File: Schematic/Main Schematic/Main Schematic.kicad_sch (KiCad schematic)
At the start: 5 parts, among them J1 Conn_01x24_Socket, J2 Conn_01x10_Pin, J3 Conn_01x24_Socket, SW1 SW_Push

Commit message: Update
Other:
- sheet Sensor ports: added 3.3V; removed none
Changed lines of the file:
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@@
-    (stroke (width 0) (type default))
-  )
-  (wire (pts (xy 250.19 43.18) (xy 255.27 43.18))
     (stroke (width 0) (type default))
   )
@@
   )
   (wire (pts (xy 250.19 53.34) (xy 255.27 53.34))
+    (stroke (width 0) (type default))
+  )
+  (wire (pts (xy 250.19 43.18) (xy 255.2192 43.18))
     (stroke (width 0) (type default))
   )
@@
     (effects (font (size 1.27 1.27)) (justify left bottom))
   )
-  (label "PB7" (at 255.27 43.18 0) (fields_autoplaced)
-    (effects (font (size 1.27 1.27)) (justify left bottom))
-    (property "Intersheetrefs" "${INTERSHEET_REFS}" (at 259.8611 43.18 0)
+  (label "PB7" (at 255.2192 43.18 0) (fields_autoplaced)
+    (effects (font (size 1.27 1.27)) (justify left bottom))
+    (property "Intersheetrefs" "${INTERSHEET_REFS}" (at 259.8103 43.18 0)
       (effects (font (size 1.27 1.27)) (justify left) hide)
     )
@@
       (effects (font (size 1.27 1.27)) hide)
     )
+  )
+  (label "3.3V" (at 63.8048 97.7392 0) (fields_autoplaced)
+    (effects (font (size 1.27 1.27)) (justify left bottom))
   )
   (label "BOOT" (at 269.24 40.64 0) (fields_autoplaced)
@@
       (effects (font (size 1.27 1.27)) (justify right))
     )
+    (pin "3.3V" input (at 63.8048 97.7392 90)
+      (effects (font (size 1.27 1.27)) (justify right))
+    )

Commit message: Updat
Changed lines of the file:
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@@
     (effects (font (size 1.27 1.27)) (justify right bottom))
   )
-  (label "PB1" (at 218.44 76.2 180) (fields_autoplaced)
-    (effects (font (size 1.27 1.27)) (justify right bottom))
-    (property "Intersheetrefs" "${INTERSHEET_REFS}" (at 20.32 -64.77 0)
-      (effects (font (size 1.27 1.27)) hide)
+  (label "PB1" (at 218.44 76.2 0) (fields_autoplaced)
+    (effects (font (size 1.27 1.27)) (justify left bottom))
+    (property "Intersheetrefs" "${INTERSHEET_REFS}" (at 223.0311 76.2 0)
+      (effects (font (size 1.27 1.27)) (justify left) hide)
     )
   )
@@
     )
   )
-  (label "PA7" (at 218.44 71.12 180) (fields_autoplaced)
-    (effects (font (size 1.27 1.27)) (justify right bottom))
-    (property "Intersheetrefs" "${INTERSHEET_REFS}" (at 20.32 -64.77 0)
-      (effects (font (size 1.27 1.27)) hide)
+  (label "PA7" (at 218.44 71.12 0) (fields_autoplaced)
+    (effects (font (size 1.27 1.27)) (justify left bottom))
+    (property "Intersheetrefs" "${INTERSHEET_REFS}" (at 222.8497 71.12 0)
+      (effects (font (size 1.27 1.27)) (justify left) hide)
     )
   )
@@
     (effects (font (size 1.27 1.27)) (justify right bottom))
   )
-  (label "PB0" (at 218.44 73.66 180) (fields_autoplaced)
-    (effects (font (size 1.27 1.27)) (justify right bottom))
-    (property "Intersheetrefs" "${INTERSHEET_REFS}" (at 20.32 -64.77 0)
-      (effects (font (size 1.27 1.27)) hide)
+  (label "PB0" (at 218.44 73.66 0) (fields_autoplaced)
+    (effects (font (size 1.27 1.27)) (justify left bottom))
+    (property "Intersheetrefs" "${INTERSHEET_REFS}" (at 223.0311 73.66 0)
+      (effects (font (size 1.27 1.27)) (justify left) hide)
     )
   )

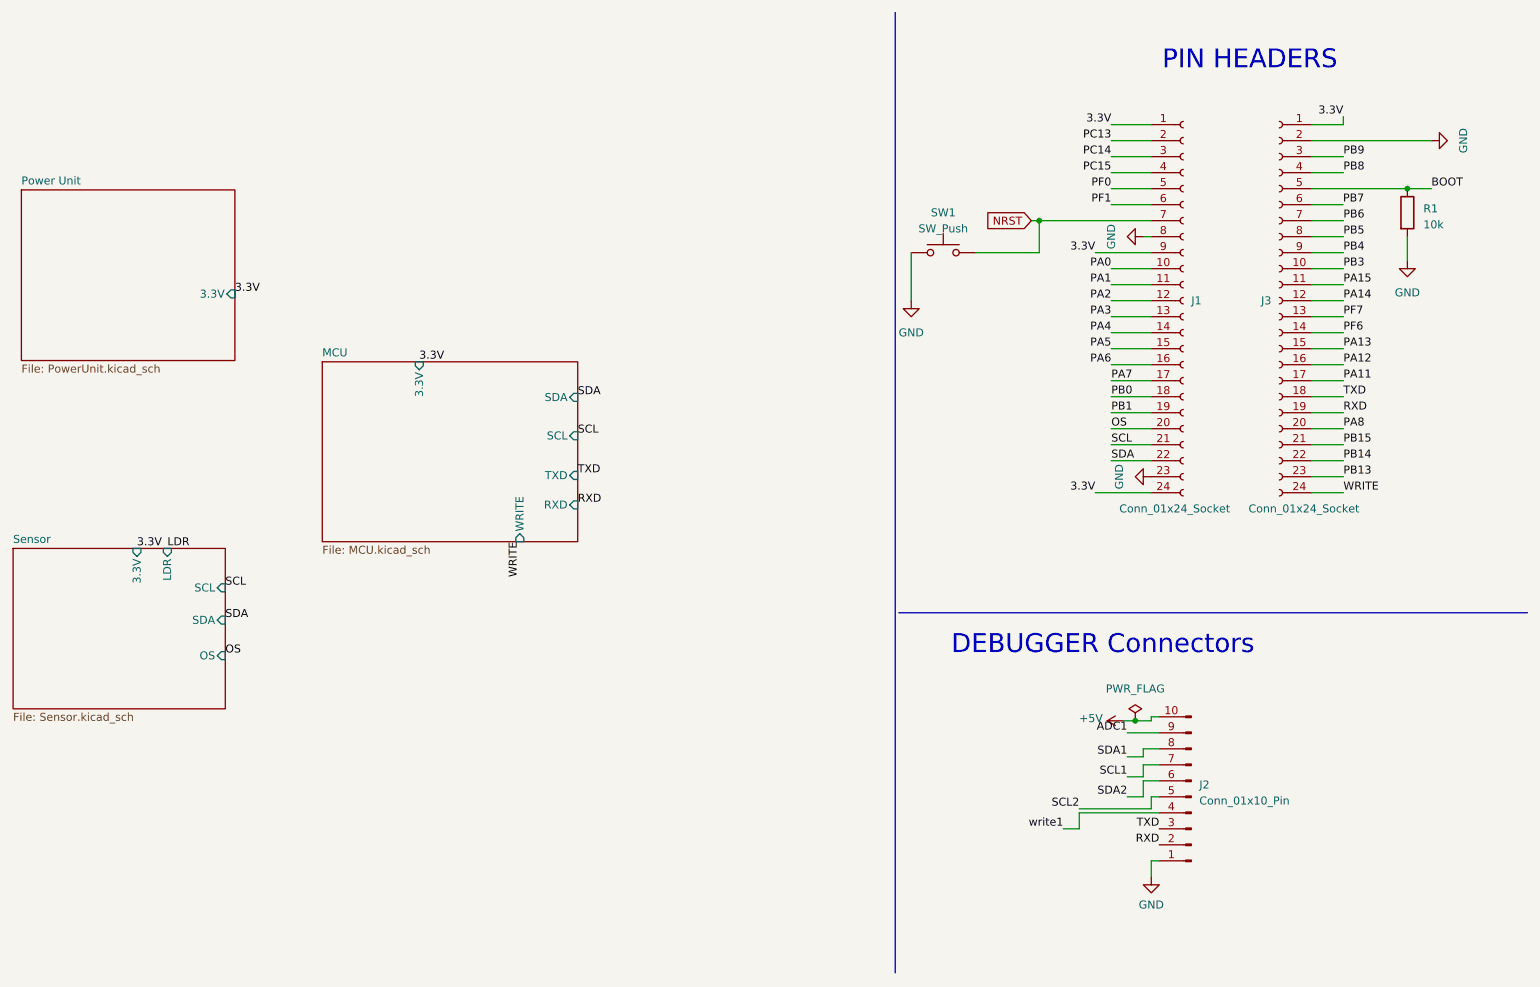
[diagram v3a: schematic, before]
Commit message: Updated the footprints and the PCB
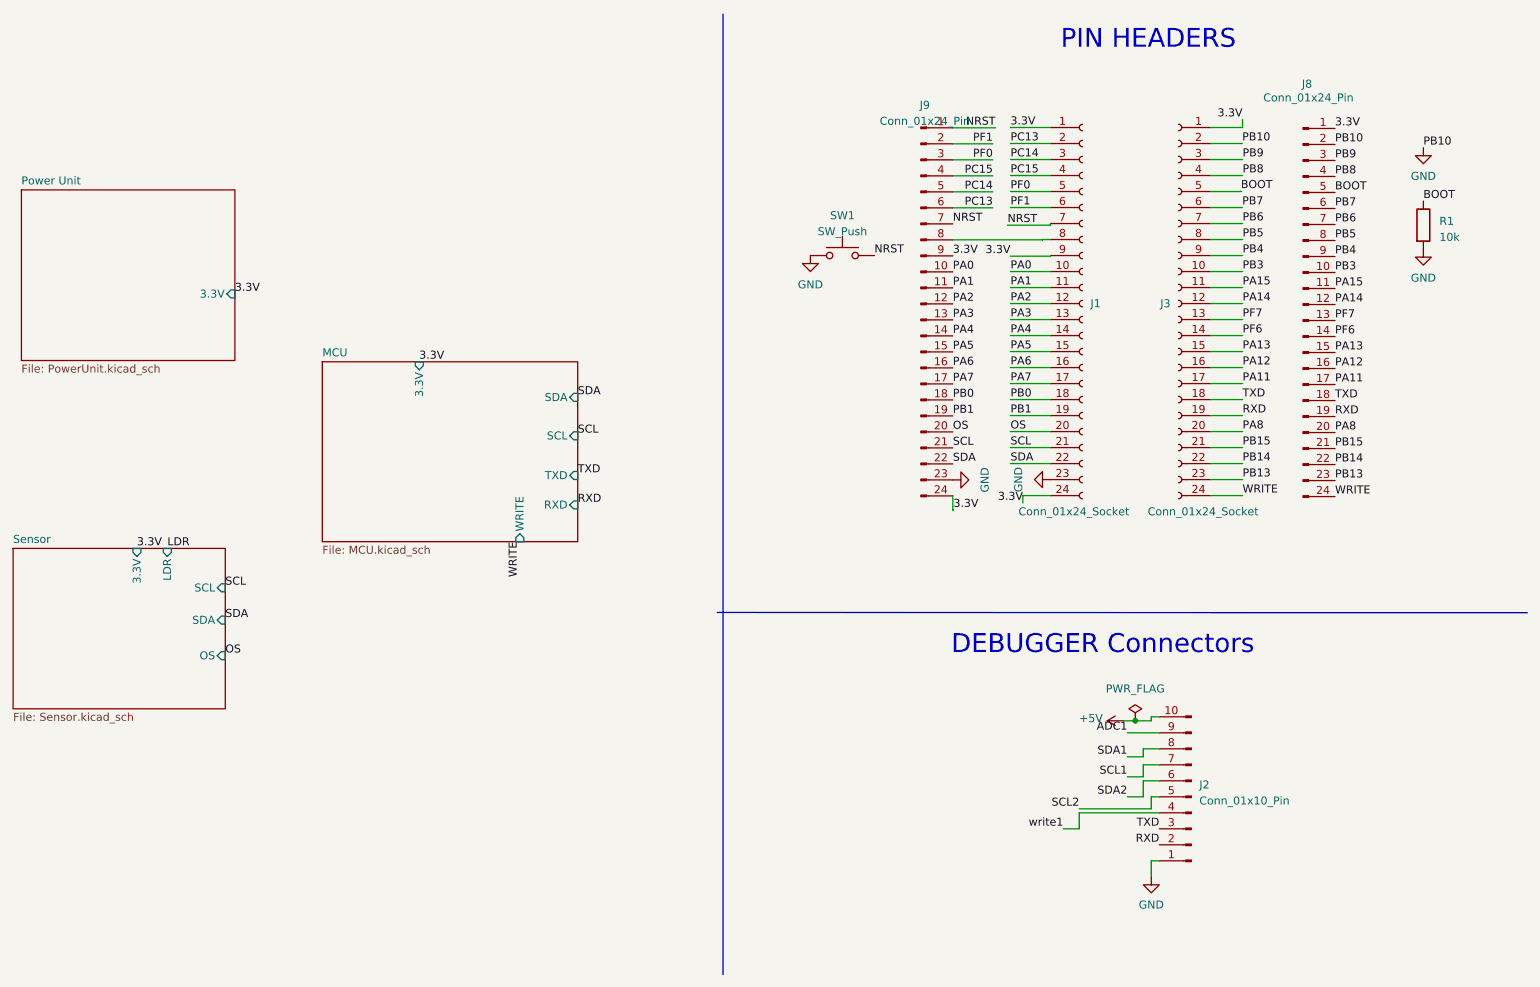
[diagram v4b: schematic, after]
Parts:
- added J8, J9: Conn_01x24_Pin, Connector_PinHeader_2.54mm:PinHeader_1x24_P2.54mm_Vertical, symbol Connector:Conn_01x24_Pin
- J1, J3: footprint (none) -> Connector_PinSocket_2.54mm:PinSocket_1x24_P2.54mm_Vertical
- J2: footprint (none) -> Connector_PinHeader_2.54mm:PinHeader_1x10_P2.54mm_Vertical
- R1: footprint (none) -> Resistor_SMD:R_1206_3216Metric
- SW1: footprint (none) -> Button_Switch_THT:Push_E-Switch_KS01Q01
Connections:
- net 3.3V: now also J8.1 (Pin_1), J9.24 (Pin_24), J9.9 (Pin_9)
- net BOOT: now also J8.5 (Pin_5)
- net GND: now also J8.2 (Pin_2), J9.23 (Pin_23); no longer J1.8 (Pin_8)
- net NRST: now also J9.1 (Pin_1), J9.7 (Pin_7)
- net OS: now also J9.20 (Pin_20)
- net PA0: now also J9.10 (Pin_10)
- net PA1: now also J9.11 (Pin_11)
- net PA11: now also J8.17 (Pin_17)
- net PA12: now also J8.16 (Pin_16)
- net PA13: now also J8.15 (Pin_15)
- net PA14: now also J8.12 (Pin_12)
- net PA15: now also J8.11 (Pin_11)
- net PA2: now also J9.12 (Pin_12)
- net PA3: now also J9.13 (Pin_13)
- net PA4: now also J9.14 (Pin_14)
- net PA5: now also J9.15 (Pin_15)
- net PA6: now also J9.16 (Pin_16)
- net PA7: now also J9.17 (Pin_17)
- net PA8: now also J8.20 (Pin_20)
- net PB0: now also J9.18 (Pin_18)
- net PB1: now also J9.19 (Pin_19)
- net PB13: now also J8.23 (Pin_23)
- net PB14: now also J8.22 (Pin_22)
- net PB15: now also J8.21 (Pin_21)
- net PB3: now also J8.10 (Pin_10)
- net PB4: now also J8.9 (Pin_9)
- net PB5: now also J8.8 (Pin_8)
- net PB6: now also J8.7 (Pin_7)
- net PB7: now also J8.6 (Pin_6)
- net PB8: now also J8.4 (Pin_4)
- net PB9: now also J8.3 (Pin_3)
- net PC13: now also J9.6 (Pin_6)
- net PC14: now also J9.5 (Pin_5)
- net PC15: now also J9.4 (Pin_4)
- net PF0: now also J9.3 (Pin_3)
- net PF1: now also J9.2 (Pin_2)
- net PF6: now also J8.14 (Pin_14)
- net PF7: now also J8.13 (Pin_13)
- net RXD: now also J8.19 (Pin_19)
- net SCL: now also J9.21 (Pin_21)
- net SDA: now also J9.22 (Pin_22)
- net TXD: now also J8.18 (Pin_18)
- net WRITE: now also J8.24 (Pin_24)
- new net: J1.8 (Pin_8), J9.8 (Pin_8)
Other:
- moved on the sheet: J1, J3, R1, SW1

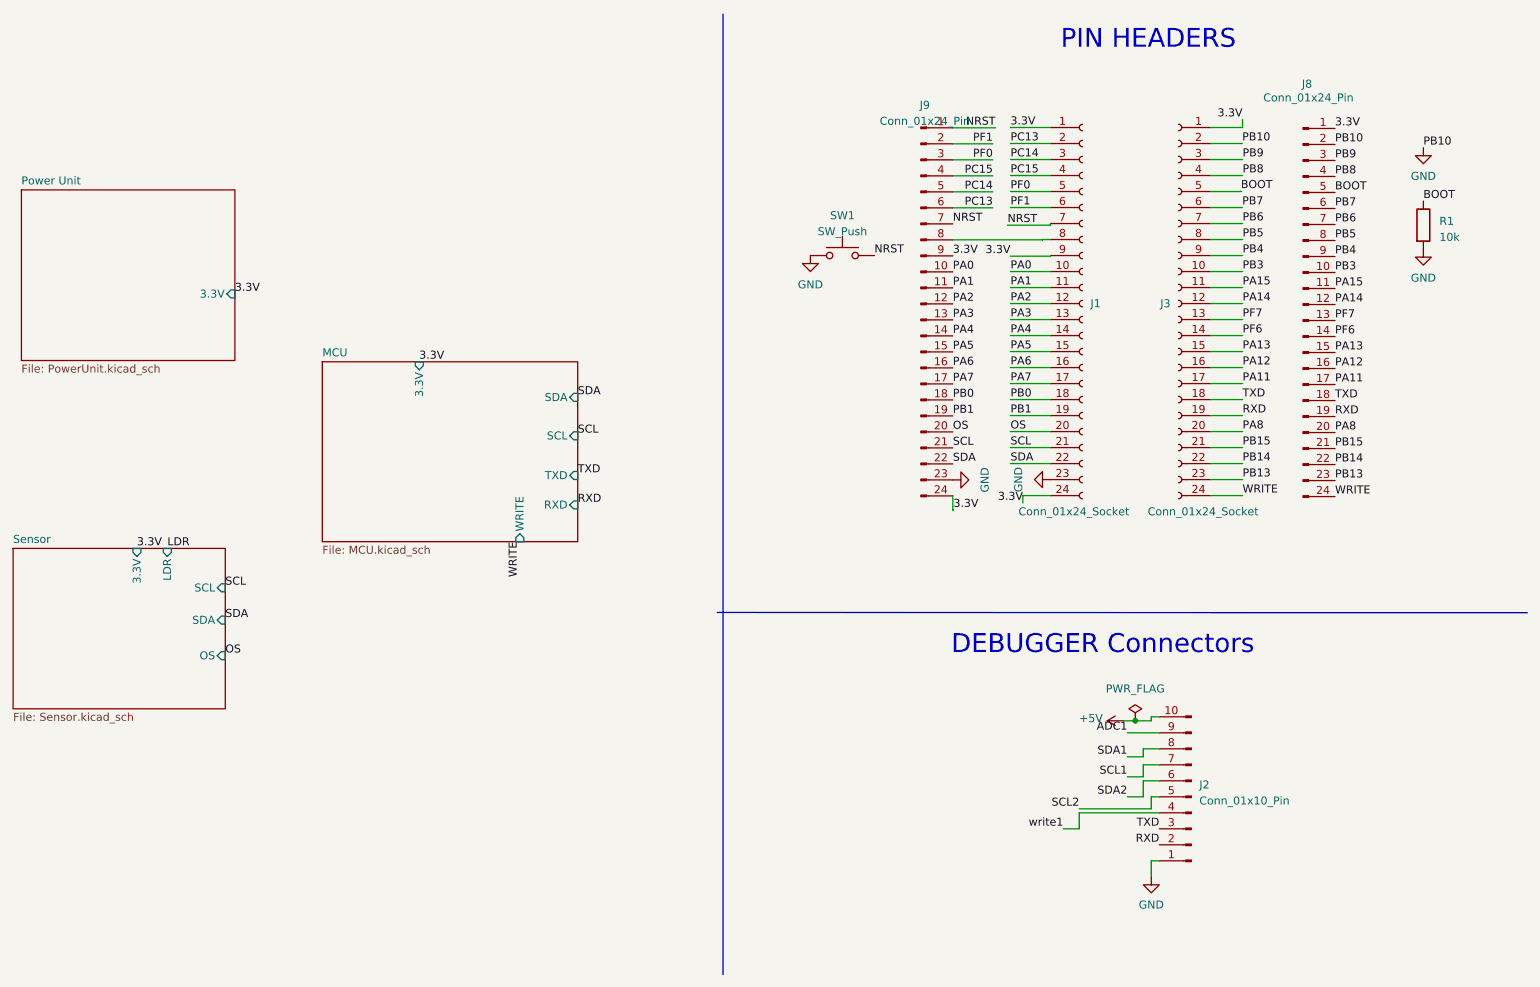
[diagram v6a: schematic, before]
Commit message: Footprints all added and the PCB has been created but not placed according to the proper configuration
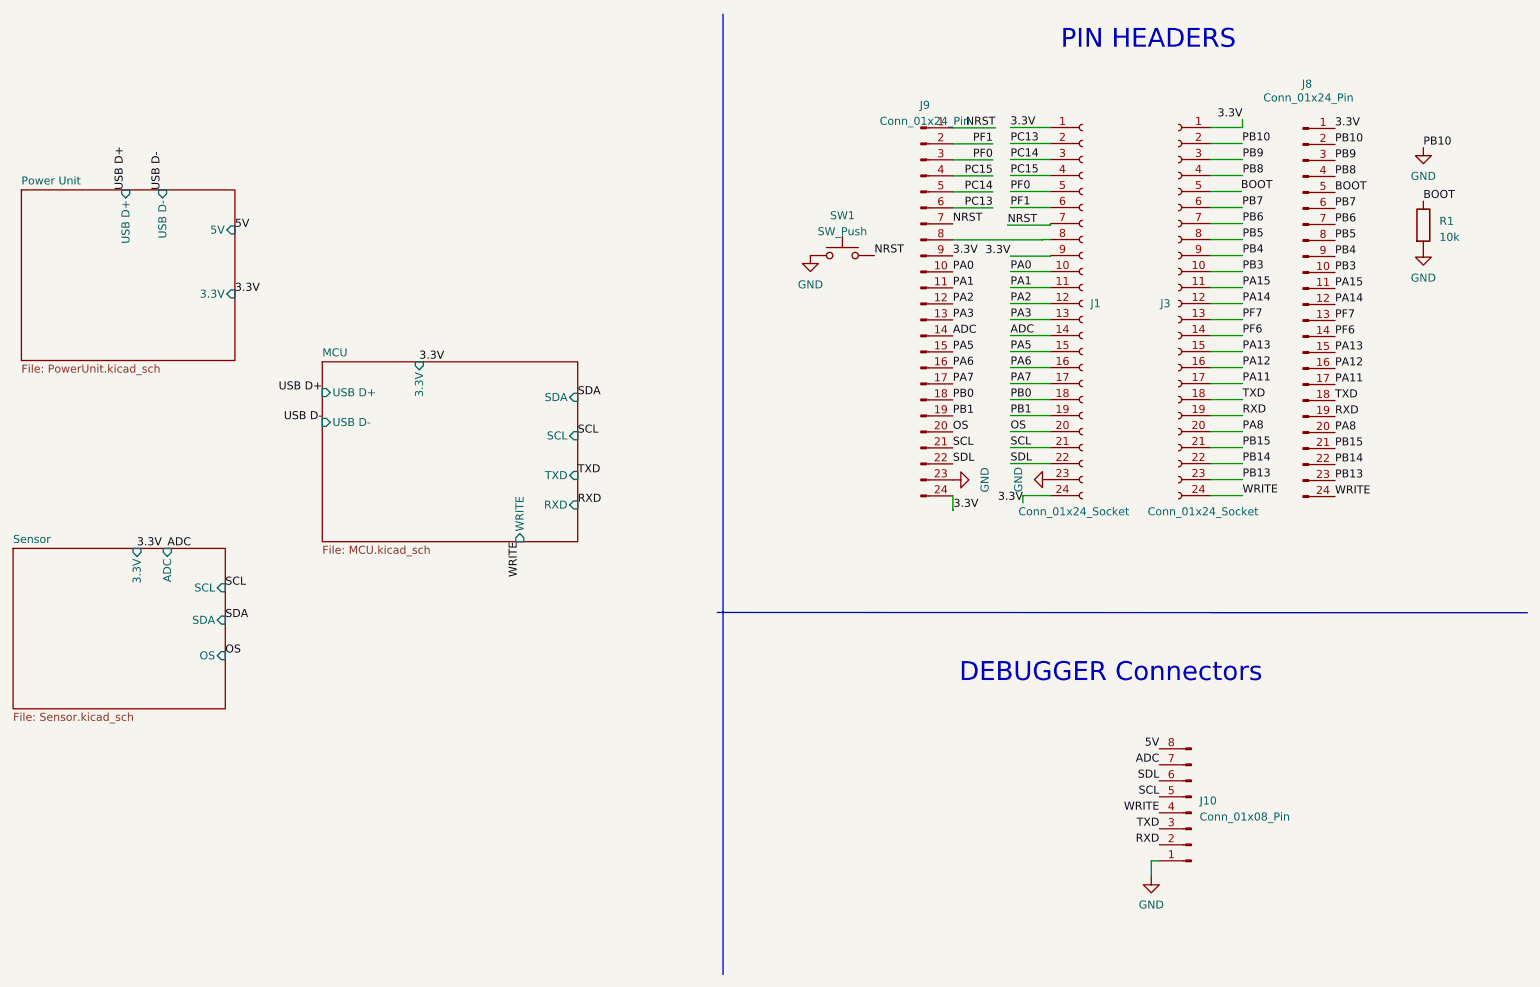
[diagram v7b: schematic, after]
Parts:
- removed J2: Conn_01x10_Pin, Connector_PinHeader_2.54mm:PinHeader_1x10_P2.54mm_Vertical, symbol Connector:Conn_01x10_Pin
- added J10: Conn_01x08_Pin, Connector_PinHeader_2.54mm:PinHeader_1x08_P2.54mm_Vertical, symbol Connector:Conn_01x08_Pin
- SW1: footprint Button_Switch_THT:Push_E-Switch_KS01Q01 -> Button_Switch_THT:SW_PUSH_6mm
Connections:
- net GND: now also J10.1 (Pin_1)
- net RXD: now also J10.2 (Pin_2)
- net SCL: now also J10.5 (Pin_5)
- net SDA: no longer J1.22 (Pin_22), J9.22 (Pin_22)
- net TXD: now also J10.3 (Pin_3)
- net WRITE: now also J10.4 (Pin_4)
- net PA4 renamed ADC
- net ADC: now also J10.7 (Pin_7)
- new net 5V: J10.8 (Pin_8)
- new net SDL: J1.22 (Pin_22), J10.6 (Pin_6), J9.22 (Pin_22)
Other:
- sheet MCU ports: added USB D+, USB D-; removed none
- sheet Power Unit ports: added 5V, USB D+, USB D-; removed none
- sheet Sensor ports: added ADC; removed LDR

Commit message: Update
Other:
- sheet MCU ports: added SDL; removed SDA
- sheet Sensor ports: added SDL; removed SDA
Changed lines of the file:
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@@
     )
   )
-  (label "SDA" (at 77.8256 109.1184 0) (fields_autoplaced)
+  (label "SDL" (at 77.8256 109.1184 0) (fields_autoplaced)
     (effects (font (size 1.27 1.27)) (justify left bottom))
   )
@@
     )
   )
-  (label "SDA" (at 133.7564 73.7616 0) (fields_autoplaced)
+  (label "SDL" (at 133.7564 73.7616 0) (fields_autoplaced)
     (effects (font (size 1.27 1.27)) (justify left bottom))
   )
@@
       (effects (font (size 1.27 1.27)) (justify right))
     )
-    (pin "SDA" input (at 77.8256 109.1184 0)
+    (pin "SDL" input (at 77.8256 109.1184 0)
       (effects (font (size 1.27 1.27)) (justify right))
     )
@@
       (effects (font (size 1.27 1.27)) (justify left top))
     )
-    (pin "SDA" input (at 133.7564 73.7616 0)
+    (pin "SDL" input (at 133.7564 73.7616 0)
       (effects (font (size 1.27 1.27)) (justify right))
     )
